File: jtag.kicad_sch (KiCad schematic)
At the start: 37 parts, among them J4 USB_C_Receptacle_USB2.0_16P, U1 FT2232HL, U4 93AA46BT-iOT, X1 12MHz

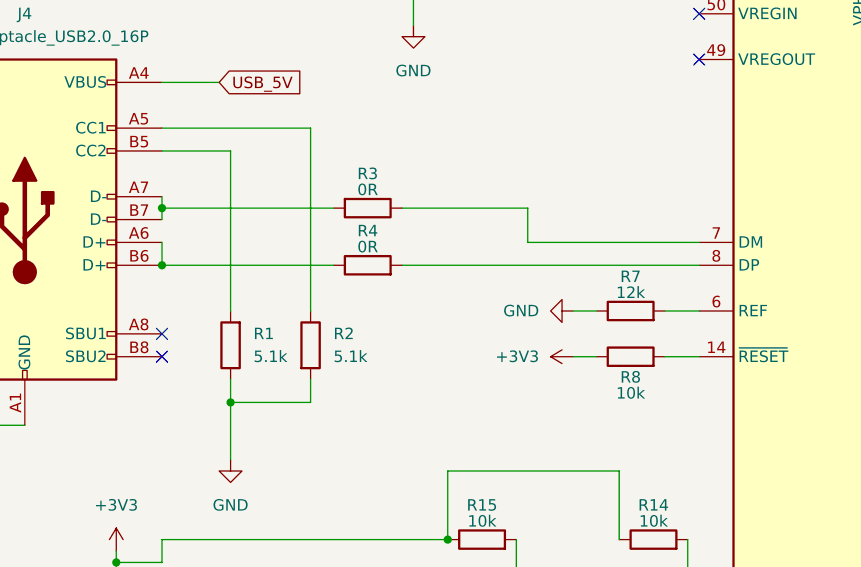
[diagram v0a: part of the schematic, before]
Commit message: Adicionando novos datasheets e comecando power
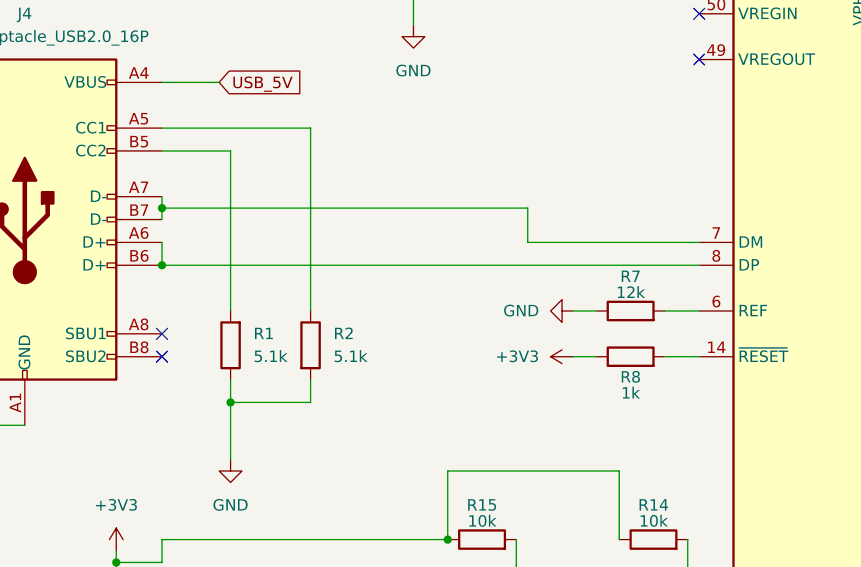
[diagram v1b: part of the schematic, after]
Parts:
- removed R3, R4: 0R, symbol Device:R
- R8: value 10k -> 1k
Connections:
- net at J4.A6 (D+), J4.B6 (D+): now also U1.8 (DP)
- net at J4.A7 (D-), J4.B7 (D-): now also U1.7 (DM)
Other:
- title: ECP5 85F Platonic Board -> PatchLogic 85 FPGA Board
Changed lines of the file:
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@@
 	(paper "A4")
 	(title_block
-		(title "ECP5 85F Platonic Board")
+		(title "PatchLogic 85 FPGA Board")
+		(date "2025-01-06")
 		(rev "V0.1")
 		(company "ODHIN Unicamp")
@@
 	(wire
 		(pts
-			(xy 67.31 72.39) (xy 48.26 72.39)
+			(xy 48.26 72.39) (xy 107.95 72.39)
 		)
 		(stroke
@@
 	(wire
 		(pts
-			(xy 74.93 66.04) (xy 88.9 66.04)
-		)
-		(stroke
-			(width 0)
-			(type default)
-		)
-	)
-	(wire
-		(pts
 			(xy 82.55 34.29) (xy 93.98 34.29)
 		)
@@
 	(wire
 		(pts
-			(xy 67.31 66.04) (xy 48.26 66.04)
+			(xy 48.26 66.04) (xy 88.9 66.04)
 		)
 		(stroke
@@
 	(wire
 		(pts
-			(xy 74.93 72.39) (xy 107.95 72.39)
-		)
-		(stroke
-			(width 0)
-			(type default)
-		)
-	)
-	(wire
-		(pts
 			(xy 66.04 133.35) (xy 66.04 129.54)
 		)
@@
 	)
 	(symbol
-		(lib_id "Device:R")
-		(at 71.12 72.39 90)
-		(unit 1)
-		(exclude_from_sim no)
-		(in_bom yes)
-		(on_board yes)
-		(dnp no)
-		(property "Reference" "R4"
-			(at 71.12 68.58 90)
-			(effects
-				(font
-					(size 1.27 1.27)
-				)
-			)
-		)
-		(property "Value" "0R"
-			(at 71.12 70.358 90)
-			(effects
-				(font
-					(size 1.27 1.27)
-				)
-			)
-		)
-		(property "Footprint" ""
-			(at 71.12 74.168 90)
-			(effects
-				(font
-					(size 1.27 1.27)
-				)
-				(hide yes)
-			)
-		)
-		(property "Datasheet" "~"
-			(at 71.12 72.39 0)
-			(effects
-				(font
-					(size 1.27 1.27)
-				)
-				(hide yes)
-			)
-		)
-		(property "Description" "Resistor"
-			(at 71.12 72.39 0)
-			(effects
-				(font
-					(size 1.27 1.27)
-				)
-				(hide yes)
-			)
-		)
-		(pin "2"
-		)
-		(pin "1"
-		)
-		(instances
-			(project ""
-				(path "/89c80bd2-25b6-4ea0-946a-21e1eb7d862c/24172778-4f65-429e-b4bb-b2e5f0d92b3f"
-					(reference "R4")
-					(unit 1)
-				)
-			)
-		)
-	)
-	(symbol
 		(lib_id "power:GND")
 		(at 25.4 93.98 0)
@@
 	)
 	(symbol
-		(lib_id "Device:R")
-		(at 71.12 66.04 270)
-		(unit 1)
-		(exclude_from_sim no)
-		(in_bom yes)
-		(on_board yes)
-		(dnp no)
-		(property "Reference" "R3"
-			(at 71.12 62.23 90)
-			(effects
-				(font
-					(size 1.27 1.27)
-				)
-			)
-		)
-		(property "Value" "0R"
-			(at 71.12 64.008 90)
-			(effects
-				(font
-					(size 1.27 1.27)
-				)
-			)
-		)
-		(property "Footprint" ""
-			(at 71.12 64.262 90)
-			(effects
-				(font
-					(size 1.27 1.27)
-				)
-				(hide yes)
-			)
-		)
-		(property "Datasheet" "~"
-			(at 71.12 66.04 0)
-			(effects
-				(font
-					(size 1.27 1.27)
-				)
-				(hide yes)
-			)
-		)
-		(property "Description" "Resistor"
-			(at 71.12 66.04 0)
-			(effects
-				(font
-					(size 1.27 1.27)
-				)
-				(hide yes)
-			)
-		)
-		(pin "2"
-		)
-		(pin "1"
-		)
-		(instances
-			(project ""
-				(path "/89c80bd2-25b6-4ea0-946a-21e1eb7d862c/24172778-4f65-429e-b4bb-b2e5f0d92b3f"
-					(reference "R3")
-					(unit 1)
-				)
-			)
-		)
-	)
-	(symbol
 		(lib_id "power:GND")
 		(at 55.88 93.98 0)
@@
 			)
 		)
-		(property "Value" "10k"
+		(property "Value" "1k"
 			(at 100.33 86.614 90)
 			(effects

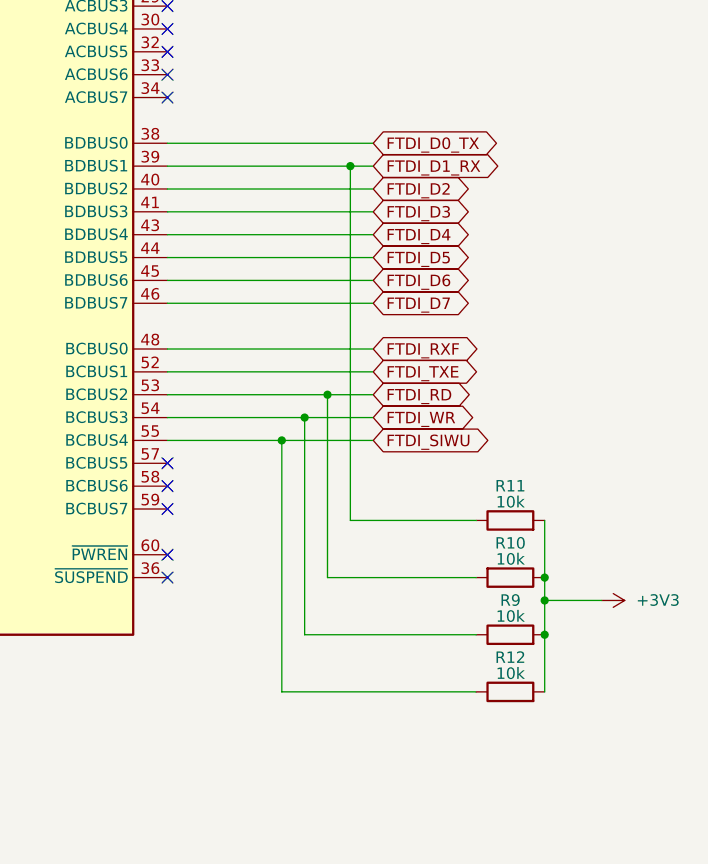
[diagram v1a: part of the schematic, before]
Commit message: Implementando power e ligando jtag e flash a fpga
Implementando circuito de power. Ligando JTAG e memoria FLASH quad SPI a
FPGA. Iniciando implementacão da DRAM e outros modulos
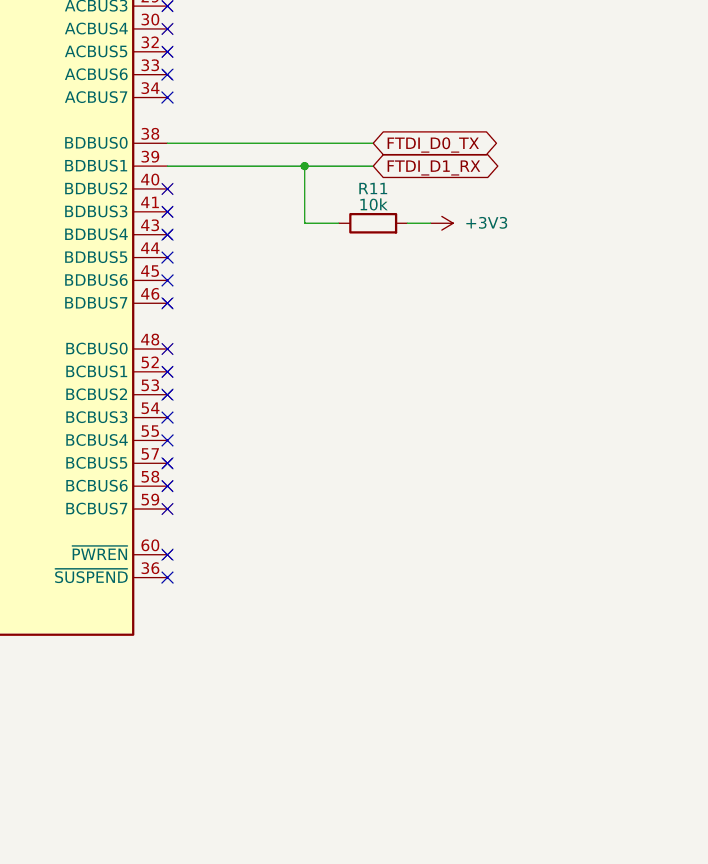
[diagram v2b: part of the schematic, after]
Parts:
- removed R10, R12, R9: 10k, symbol Device:R
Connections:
- net FTDI_D2: no longer names the net of U1.40 (BDBUS2)
- net FTDI_D3: no longer names the net of U1.41 (BDBUS3)
- net FTDI_D4: no longer names the net of U1.43 (BDBUS4)
- net FTDI_D5: no longer names the net of U1.44 (BDBUS5)
- net FTDI_D6: no longer names the net of U1.45 (BDBUS6)
- net FTDI_D7: no longer names the net of U1.46 (BDBUS7)
- net FTDI_RD: no longer names the net of U1.53 (BCBUS2)
- net FTDI_RXF: no longer names the net of U1.48 (BCBUS0)
- net FTDI_SIWU: no longer names the net of U1.55 (BCBUS4)
- net FTDI_TXE: no longer names the net of U1.52 (BCBUS1)
- net FTDI_WR: no longer names the net of U1.54 (BCBUS3)
- no-connect marks 22 -> 33
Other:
- moved on the sheet: R11
